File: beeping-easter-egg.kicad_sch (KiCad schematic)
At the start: 14 parts, among them Q1 AO3401A, Q2 AO3401A, SW1 SW_SPDT, U1 TLC555xD

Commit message: Add footprints for battery holder and switch using easyeda2kicad script.
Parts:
- BT1: footprint (none) -> easyeda2kicad:BAT-TH_BS-04-A1BJ004
- SW1: footprint (none) -> easyeda2kicad:SW-TH_3P-L8.3-W5.2-P2.54_ST-0-102-A01-T000
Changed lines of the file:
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@@
 			)
 		)
-		(property "Footprint" ""
+		(property "Footprint" "easyeda2kicad:BAT-TH_BS-04-A1BJ004"
 			(at 48.26 87.376 90)
 			(effects
@@
 			)
 		)
-		(property "Footprint" ""
+		(property "Footprint" "easyeda2kicad:SW-TH_3P-L8.3-W5.2-P2.54_ST-0-102-A01-T000"
 			(at 48.26 76.2 0)
 			(effects

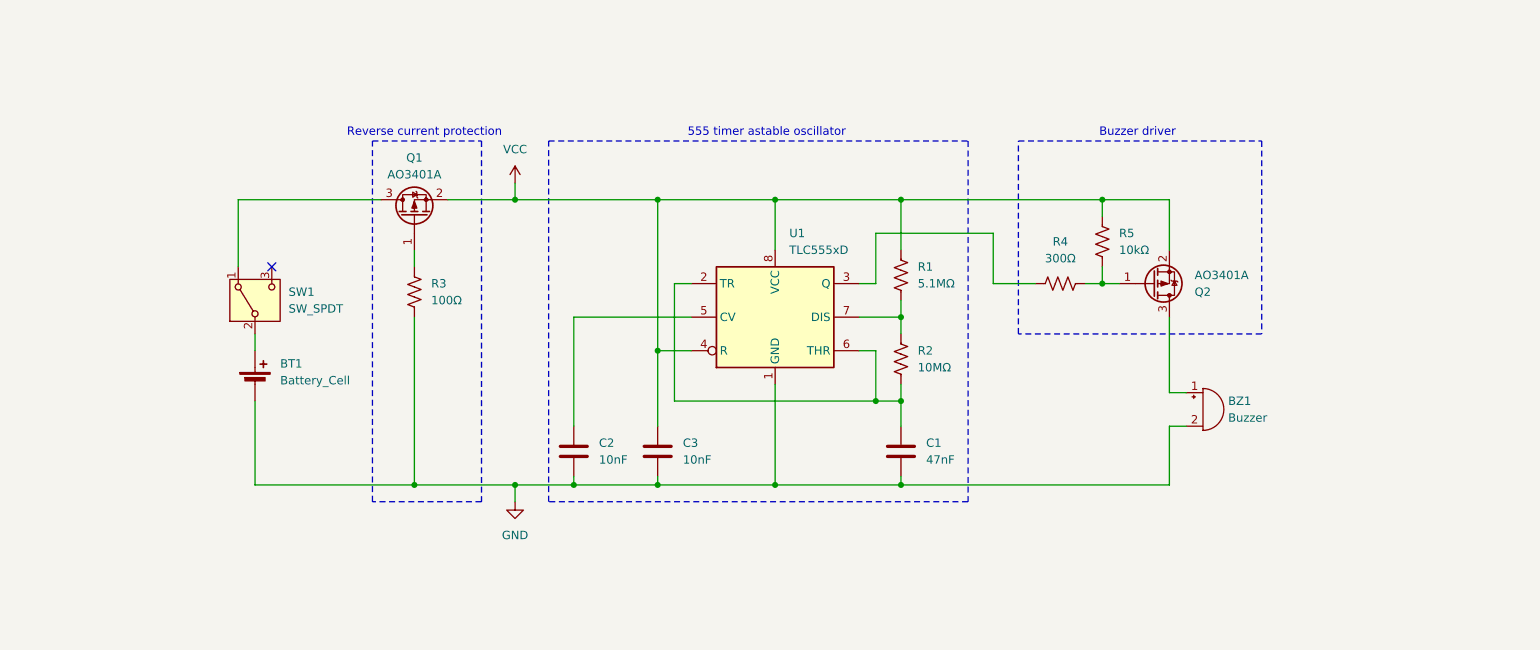
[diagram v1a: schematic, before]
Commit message: Clean up fab layers. Update some component info.
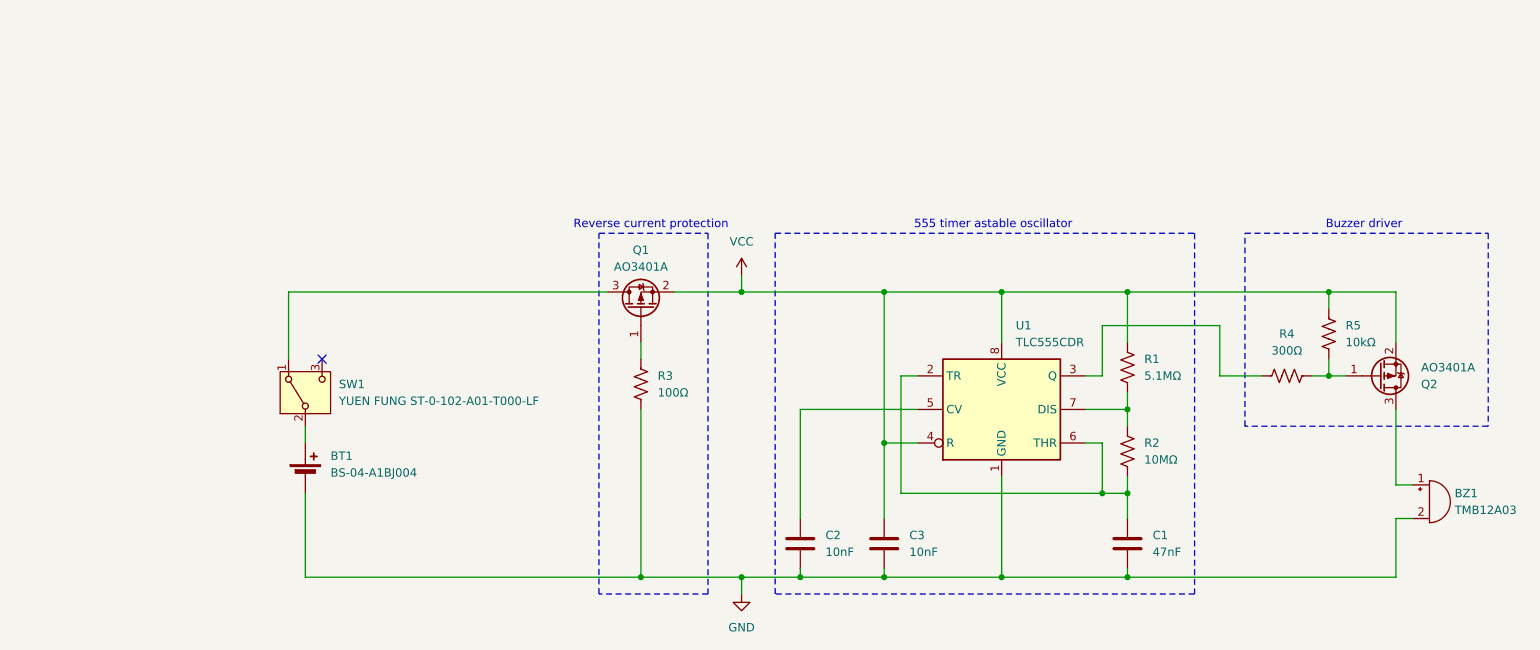
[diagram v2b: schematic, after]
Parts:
- BT1: value Battery_Cell -> BS-04-A1BJ004
- BZ1: value Buzzer -> TMB12A03
- SW1: value SW_SPDT -> YUEN FUNG ST-0-102-A01-T000-LF
- U1: value TLC555xD -> TLC555CDR
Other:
- moved on the sheet: BT1, BZ1, C1, C2, C3, Q1, Q2, R1, R2, R3, R4, R5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

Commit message: Resize schematic to A5. Add title to schematic.
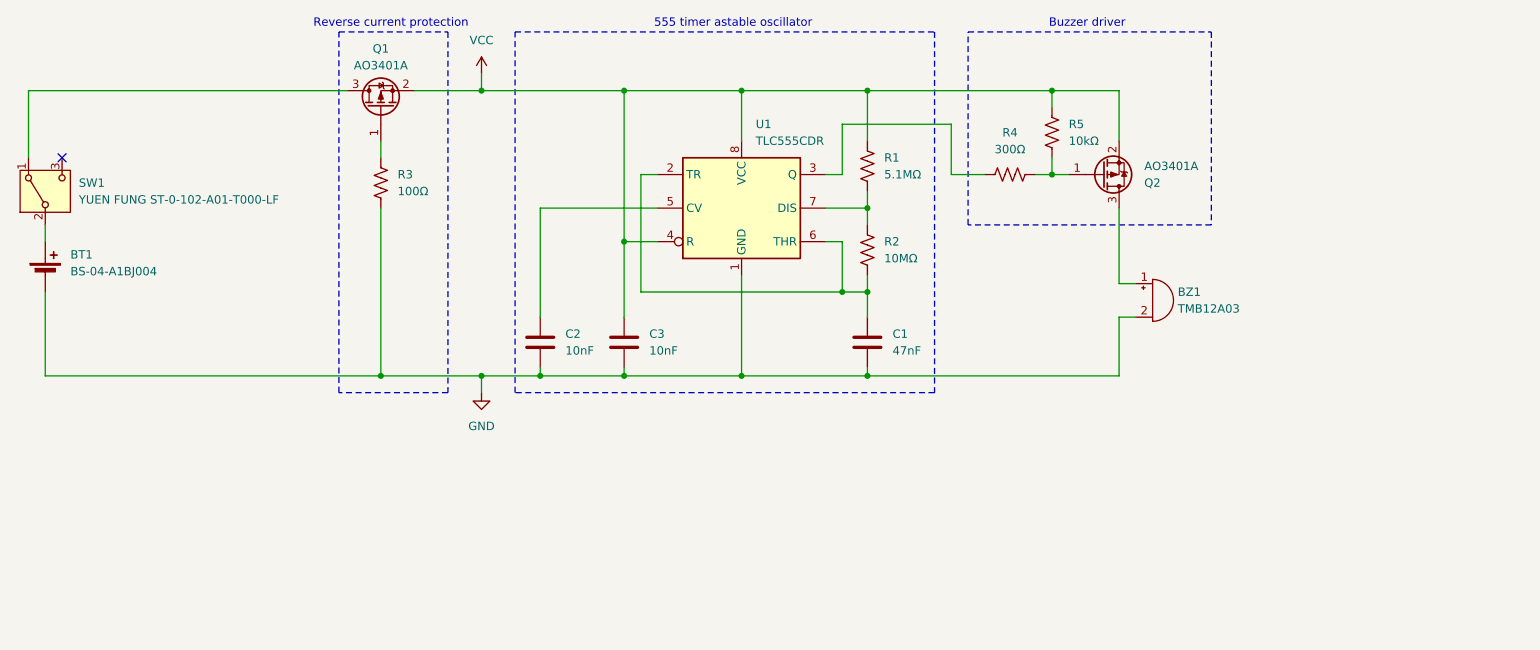
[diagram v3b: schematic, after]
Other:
- title: (none) -> github.com/DougTomanio/beeping-easter-egg
- moved on the sheet: BT1, BZ1, C1, C2, C3, Q1, Q2, R1, R2, R3, R4, R5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

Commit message: Fix missing ref DRC issue with tooling holes
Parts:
- added H1, H2, H3: MountingHole, MountingHole:ToolingHole_1.152mm, symbol Mechanical:MountingHole
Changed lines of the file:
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@@
+	)
+	(symbol
+		(lib_id "Mechanical:MountingHole")
+		(at 49.53 105.41 0)
+		(unit 1)
+		(exclude_from_sim yes)
+		(in_bom no)
+		(on_board yes)
+		(dnp no)
+		(fields_autoplaced yes)
+		(property "Reference" "H1"
+			(at 52.07 104.1399 0)
+			(effects
+				(font
+					(size 1.27 1.27)
+				)
+				(justify left)
+			)
+		)
+		(property "Value" "MountingHole"
+			(at 52.07 106.6799 0)
+			(effects
+				(font
+					(size 1.27 1.27)
+				)
+				(justify left)
+			)
+		)
+		(property "Footprint" "MountingHole:ToolingHole_1.152mm"
+			(at 49.53 105.41 0)
+			(effects
+				(font
+					(size 1.27 1.27)
+				)
+				(hide yes)
+			)
+		)
+		(property "Datasheet" "~"
+			(at 49.53 105.41 0)
+			(effects
+				(font
+					(size 1.27 1.27)
+				)
+				(hide yes)
+			)
+		)
+		(property "Description" "Mounting Hole without connection"
+			(at 49.53 105.41 0)
+			(effects
+				(font
+					(size 1.27 1.27)
+				)
+				(hide yes)
+			)
+		)
+		(instances
+			(project ""
+				(path "/18231612-44e3-4d58-b7d2-9123d50293a3"
+					(reference "H1")
+					(unit 1)
+				)
+			)
+		)
 	)
 	(symbol
@@
 					(unit 1)
 				)
+			)
+		)
+	)
+	(symbol
+		(lib_id "Mechanical:MountingHole")
+		(at 49.53 115.57 0)
+		(unit 1)
+		(exclude_from_sim yes)
+		(in_bom no)
+		(on_board yes)
+		(dnp no)
+		(fields_autoplaced yes)
+		(property "Reference" "H3"
+			(at 52.07 114.2999 0)
+			(effects
+				(font
+					(size 1.27 1.27)
+				)
+				(justify left)
+			)
+		)
+		(property "Value" "MountingHole"
+			(at 52.07 116.8399 0)
+			(effects
+				(font
+					(size 1.27 1.27)
+				)
+				(justify left)
+			)
+		)
+		(property "Footprint" "MountingHole:ToolingHole_1.152mm"
+			(at 49.53 115.57 0)
+			(effects
+				(font
+					(size 1.27 1.27)
+				)
+				(hide yes)
+			)
+		)
+		(property "Datasheet" "~"
+			(at 49.53 115.57 0)
+			(effects
+				(font
+					(size 1.27 1.27)
+				)
+				(hide yes)
+			)
+		)
+		(property "Description" "Mounting Hole without connection"
+			(at 49.53 115.57 0)
+			(effects
+				(font
+					(size 1.27 1.27)
+				)
+				(hide yes)
+			)
+		)
+		(instances
+			(project ""
+				(path "/18231612-44e3-4d58-b7d2-9123d50293a3"
+					(reference "H3")
+					(unit 1)
+				)
+			)
+		)
+	)
+	(symbol
+		(lib_id "Mechanical:MountingHole")
+		(at 49.53 110.49 0)
+		(unit 1)
+		(exclude_from_sim yes)
+		(in_bom no)
+		(on_board yes)
+		(dnp no)
+		(fields_autoplaced yes)
+		(property "Reference" "H2"
+			(at 52.07 109.2199 0)
+			(effects
+				(font
+					(size 1.27 1.27)
+				)
+				(justify left)
+			)
+		)
+		(property "Value" "MountingHole"
+			(at 52.07 111.7599 0)
+			(effects
+				(font
+					(size 1.27 1.27)
+				)
+				(justify left)
+			)
+		)
+		(property "Footprint" "MountingHole:ToolingHole_1.152mm"
+			(at 49.53 110.49 0)
+			(effects
+				(font
+					(size 1.27 1.27)
+				)
+				(hide yes)
+			)
+		)
+		(property "Datasheet" "~"
+			(at 49.53 110.49 0)
+			(effects
+				(font
+					(size 1.27 1.27)
+				)
+				(hide yes)
+			)
+		)
+		(property "Description" "Mounting Hole without connection"
+			(at 49.53 110.49 0)
+			(effects
+				(font
+					(size 1.27 1.27)
+				)
+				(hide yes)
+			)
+		)
+		(instances
+			(project ""
+				(path "/18231612-44e3-4d58-b7d2-9123d50293a3"
+					(reference "H2")
+					(unit 1)
+				)

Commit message: Move component info generated by easyeda2kicad to local project library.
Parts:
- BT1: footprint easyeda2kicad:BAT-TH_BS-04-A1BJ004 -> Library:BAT-TH_BS-04-A1BJ004
- SW1: footprint easyeda2kicad:SW-TH_3P-L8.3-W5.2-P2.54_ST-0-102-A01-T000 -> Library:SW-TH_3P-L8.3-W5.2-P2.54_ST-0-102-A01-T000
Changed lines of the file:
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@@
 			)
 		)
-		(property "Footprint" "easyeda2kicad:BAT-TH_BS-04-A1BJ004"
+		(property "Footprint" "Library:BAT-TH_BS-04-A1BJ004"
 			(at 16.51 70.866 90)
 			(effects
@@
 			)
 		)
-		(property "Footprint" "easyeda2kicad:SW-TH_3P-L8.3-W5.2-P2.54_ST-0-102-A01-T000"
+		(property "Footprint" "Library:SW-TH_3P-L8.3-W5.2-P2.54_ST-0-102-A01-T000"
 			(at 16.51 59.69 0)
 			(effects

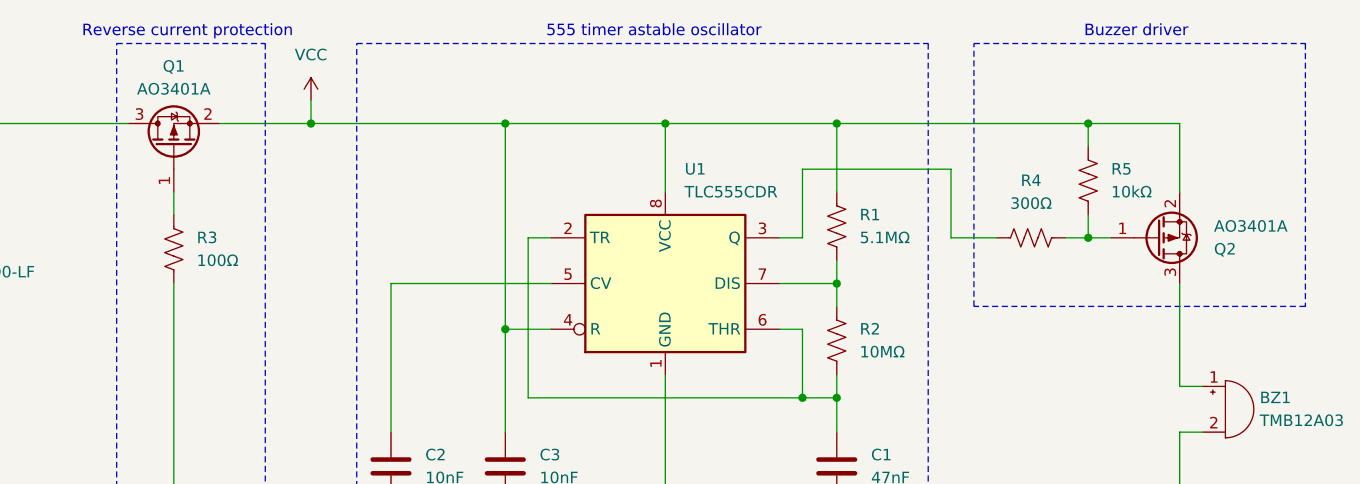
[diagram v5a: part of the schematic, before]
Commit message: Corrections for JLCPCB component rotation using KiKit "JLCPCB_CORRECTION" property
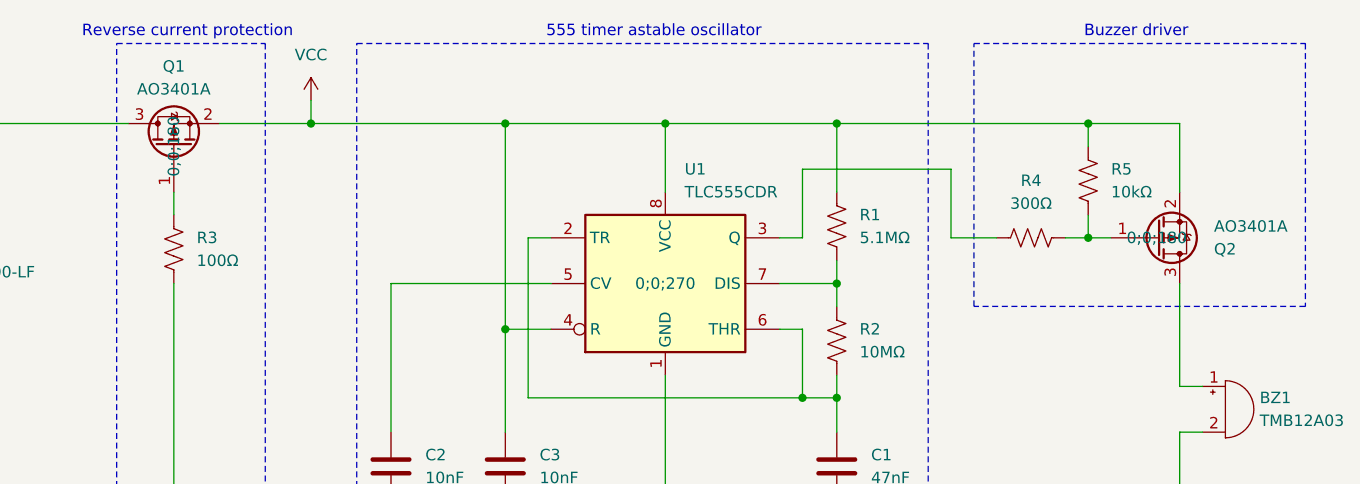
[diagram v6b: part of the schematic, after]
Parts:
- Q1, Q2: JLCPCB_CORRECTION (none) -> 0;0;180
- U1: JLCPCB_CORRECTION (none) -> 0;0;270
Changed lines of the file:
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@@
+			)
+		)
+		(property "JLCPCB_CORRECTION" ""
+			(at 16.51 72.39 0)
+			(effects
+				(font
+					(size 1.27 1.27)
+				)
 			)
 		)
@@
 			)
 		)
+		(property "JLCPCB_CORRECTION" ""
+			(at 140.97 82.55 0)
+			(effects
+				(font
+					(size 1.27 1.27)
+				)
+			)
+		)
 		(pin "2"
 		)
@@
 			)
 		)
+		(property "JLCPCB_CORRECTION" ""
+			(at 16.51 59.69 0)
+			(effects
+				(font
+					(size 1.27 1.27)
+				)
+			)
+		)
 		(pin "2"
 		)
@@
 			)
 		)
+		(property "JLCPCB_CORRECTION" ""
+			(at 140.97 55.88 0)
+			(effects
+				(font
+					(size 1.27 1.27)
+				)
+			)
+		)
 		(pin "2"
 		)
@@
 			)
 		)
+		(property "JLCPCB_CORRECTION" ""
+			(at 184.15 76.2 0)
+			(effects
+				(font
+					(size 1.27 1.27)
+				)
+			)
+		)
 		(pin "2"
 		)
@@
 			)
 		)
+		(property "JLCPCB_CORRECTION" "0;0;270"
+			(at 121.92 62.23 0)
+			(effects
+				(font
+					(size 1.27 1.27)
+				)
+			)
+		)
 		(pin "1"
 		)
@@
 			)
 		)
+		(property "JLCPCB_CORRECTION" ""
+			(at 49.53 105.41 0)
+			(effects
+				(font
+					(size 1.27 1.27)
+				)
+			)
+		)
 		(instances
 			(project ""
@@
 			)
 		)
+		(property "JLCPCB_CORRECTION" ""
+			(at 104.14 82.55 0)
+			(effects
+				(font
+					(size 1.27 1.27)
+				)
+			)
+		)
 		(pin "2"
 		)
@@
 			)
 		)
+		(property "JLCPCB_CORRECTION" ""
+			(at 168.91 50.8 0)
+			(effects
+				(font
+					(size 1.27 1.27)
+				)
+			)
+		)
 		(pin "2"
 		)
@@
 			)
 		)
+		(property "JLCPCB_CORRECTION" ""
+			(at 140.97 68.58 0)
+			(effects
+				(font
+					(size 1.27 1.27)
+				)
+			)
+		)
 		(pin "1"
 		)
@@
 			)
 		)
+		(property "JLCPCB_CORRECTION" ""
+			(at 162.56 57.15 0)
+			(effects
+				(font
+					(size 1.27 1.27)
+				)
+			)
+		)
 		(pin "2"
 		)
@@
 			)
 		)
+		(property "JLCPCB_CORRECTION" ""
+			(at 49.53 115.57 0)
+			(effects
+				(font
+					(size 1.27 1.27)
+				)
+			)
+		)
 		(instances
 			(project ""
@@
 			)
 		)
+		(property "JLCPCB_CORRECTION" ""
+			(at 49.53 110.49 0)
+			(effects
+				(font
+					(size 1.27 1.27)
+				)
+			)
+		)
 		(instances
 			(project ""
@@
 			)
 		)
+		(property "JLCPCB_CORRECTION" ""
+			(at 67.31 58.42 0)
+			(effects
+				(font
+					(size 1.27 1.27)
+				)
+			)
+		)
 		(pin "2"
 		)
@@
 				)
 				(hide yes)
+			)
+		)
+		(property "JLCPCB_CORRECTION" "0;0;180"
+			(at 67.31 46.99 0)
+			(effects
+				(font
+					(size 1.27 1.27)
+				)
 			)
 		)
@@
 			)
 		)
+		(property "JLCPCB_CORRECTION" "0;0;180"
+			(at 176.53 57.15 0)
+			(effects
+				(font
+					(size 1.27 1.27)
+				)
+			)
+		)
 		(pin "3"
 		)
@@
 			)
 		)
+		(property "JLCPCB_CORRECTION" ""
+			(at 91.44 82.55 0)
+			(effects
+				(font
+					(size 1.27 1.27)
+				)
+			)
+		)

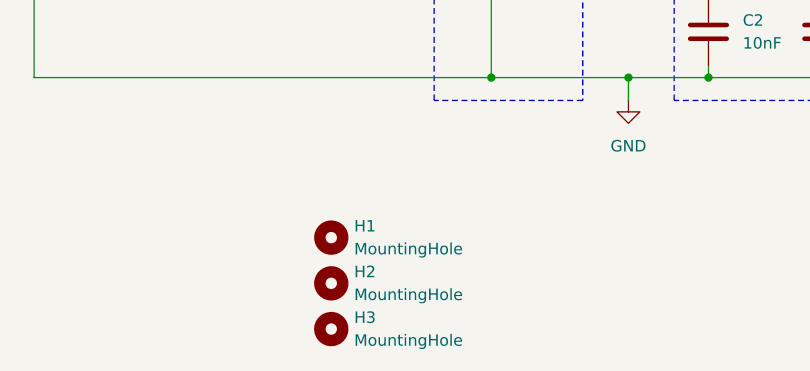
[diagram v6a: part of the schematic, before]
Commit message: Remove tooling holes. They are added to the panelization frame instead.
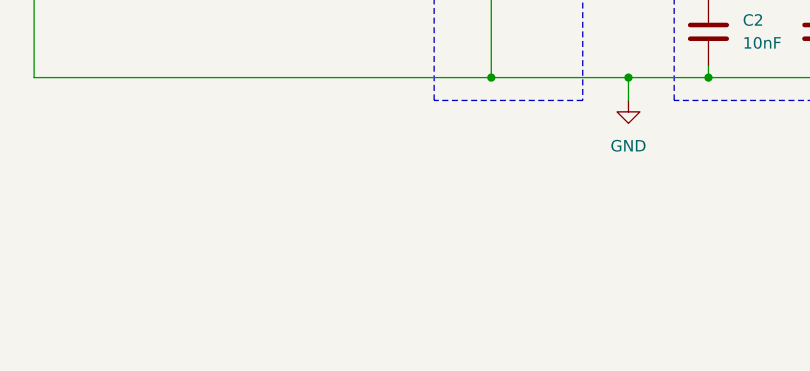
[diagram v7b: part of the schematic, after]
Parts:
- removed H1, H2, H3: MountingHole, MountingHole:ToolingHole_1.152mm, symbol Mechanical:MountingHole
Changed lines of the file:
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@@
-	)
-	(symbol
-		(lib_id "Mechanical:MountingHole")
-		(at 49.53 105.41 0)
-		(unit 1)
-		(exclude_from_sim yes)
-		(in_bom no)
-		(on_board yes)
-		(dnp no)
-		(fields_autoplaced yes)
-		(property "Reference" "H1"
-			(at 52.07 104.1399 0)
-			(effects
-				(font
-					(size 1.27 1.27)
-				)
-				(justify left)
-			)
-		)
-		(property "Value" "MountingHole"
-			(at 52.07 106.6799 0)
-			(effects
-				(font
-					(size 1.27 1.27)
-				)
-				(justify left)
-			)
-		)
-		(property "Footprint" "MountingHole:ToolingHole_1.152mm"
-			(at 49.53 105.41 0)
-			(effects
-				(font
-					(size 1.27 1.27)
-				)
-				(hide yes)
-			)
-		)
-		(property "Datasheet" "~"
-			(at 49.53 105.41 0)
-			(effects
-				(font
-					(size 1.27 1.27)
-				)
-				(hide yes)
-			)
-		)
-		(property "Description" "Mounting Hole without connection"
-			(at 49.53 105.41 0)
-			(effects
-				(font
-					(size 1.27 1.27)
-				)
-				(hide yes)
-			)
-		)
-		(property "JLCPCB_CORRECTION" ""
-			(at 49.53 105.41 0)
-			(effects
-				(font
-					(size 1.27 1.27)
-				)
-			)
-		)
-		(instances
-			(project ""
-				(path "/18231612-44e3-4d58-b7d2-9123d50293a3"
-					(reference "H1")
-					(unit 1)
-				)
-			)
-		)
 	)
 	(symbol
@@
 					(unit 1)
 				)
-			)
-		)
-	)
-	(symbol
-		(lib_id "Mechanical:MountingHole")
-		(at 49.53 115.57 0)
-		(unit 1)
-		(exclude_from_sim yes)
-		(in_bom no)
-		(on_board yes)
-		(dnp no)
-		(fields_autoplaced yes)
-		(property "Reference" "H3"
-			(at 52.07 114.2999 0)
-			(effects
-				(font
-					(size 1.27 1.27)
-				)
-				(justify left)
-			)
-		)
-		(property "Value" "MountingHole"
-			(at 52.07 116.8399 0)
-			(effects
-				(font
-					(size 1.27 1.27)
-				)
-				(justify left)
-			)
-		)
-		(property "Footprint" "MountingHole:ToolingHole_1.152mm"
-			(at 49.53 115.57 0)
-			(effects
-				(font
-					(size 1.27 1.27)
-				)
-				(hide yes)
-			)
-		)
-		(property "Datasheet" "~"
-			(at 49.53 115.57 0)
-			(effects
-				(font
-					(size 1.27 1.27)
-				)
-				(hide yes)
-			)
-		)
-		(property "Description" "Mounting Hole without connection"
-			(at 49.53 115.57 0)
-			(effects
-				(font
-					(size 1.27 1.27)
-				)
-				(hide yes)
-			)
-		)
-		(property "JLCPCB_CORRECTION" ""
-			(at 49.53 115.57 0)
-			(effects
-				(font
-					(size 1.27 1.27)
-				)
-			)
-		)
-		(instances
-			(project ""
-				(path "/18231612-44e3-4d58-b7d2-9123d50293a3"
-					(reference "H3")
-					(unit 1)
-				)
-			)
-		)
-	)
-	(symbol
-		(lib_id "Mechanical:MountingHole")
-		(at 49.53 110.49 0)
-		(unit 1)
-		(exclude_from_sim yes)
-		(in_bom no)
-		(on_board yes)
-		(dnp no)
-		(fields_autoplaced yes)
-		(property "Reference" "H2"
-			(at 52.07 109.2199 0)
-			(effects
-				(font
-					(size 1.27 1.27)
-				)
-				(justify left)
-			)
-		)
-		(property "Value" "MountingHole"
-			(at 52.07 111.7599 0)
-			(effects
-				(font
-					(size 1.27 1.27)
-				)
-				(justify left)
-			)
-		)
-		(property "Footprint" "MountingHole:ToolingHole_1.152mm"
-			(at 49.53 110.49 0)
-			(effects
-				(font
-					(size 1.27 1.27)
-				)
-				(hide yes)
-			)
-		)
-		(property "Datasheet" "~"
-			(at 49.53 110.49 0)
-			(effects
-				(font
-					(size 1.27 1.27)
-				)
-				(hide yes)
-			)
-		)
-		(property "Description" "Mounting Hole without connection"
-			(at 49.53 110.49 0)
-			(effects
-				(font
-					(size 1.27 1.27)
-				)
-				(hide yes)
-			)
-		)
-		(property "JLCPCB_CORRECTION" ""
-			(at 49.53 110.49 0)
-			(effects
-				(font
-					(size 1.27 1.27)
-				)
-			)
-		)
-		(instances
-			(project ""
-				(path "/18231612-44e3-4d58-b7d2-9123d50293a3"
-					(reference "H2")
-					(unit 1)
-				)
